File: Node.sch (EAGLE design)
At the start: 69 parts, among them J1 AVR_SPI_PRG_6NS, J2 M04X2, Q1 PMR280UN, Q2 PMR280UN, Q3 PMR280UN, U1 ATMEGA32U4, U2 BLUETOOTH-RN41", U4 L3GD20, U9 RCLAMP0502A, X1 USBSMD

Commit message: more routing
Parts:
- L1, L2: device adjacent-reality:INDUCTORVLS2016 -> adjacent-reality:INDUCTORVLS30
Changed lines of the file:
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@@
 <part name="C23" library="SparkFun" deviceset="CAP" device="0402-CAP" value="1uF"/>
 <part name="U$6" library="adjacent-reality" deviceset="LSM303DLHC" device=""/>
-<part name="L1" library="adjacent-reality" deviceset="INDUCTOR" device="VLS2016" value="4.7uH"/>
-<part name="L2" library="adjacent-reality" deviceset="INDUCTOR" device="VLS2016" value="4.7uH"/>
+<part name="L1" library="adjacent-reality" deviceset="INDUCTOR" device="VLS30" value="4.7uH"/>
+<part name="L2" library="adjacent-reality" deviceset="INDUCTOR" device="VLS30" value="4.7uH"/>
 <part name="JP1" library="SparkFun-Connectors" deviceset="M02" device="PTH" value="POWER"/>
 </parts>

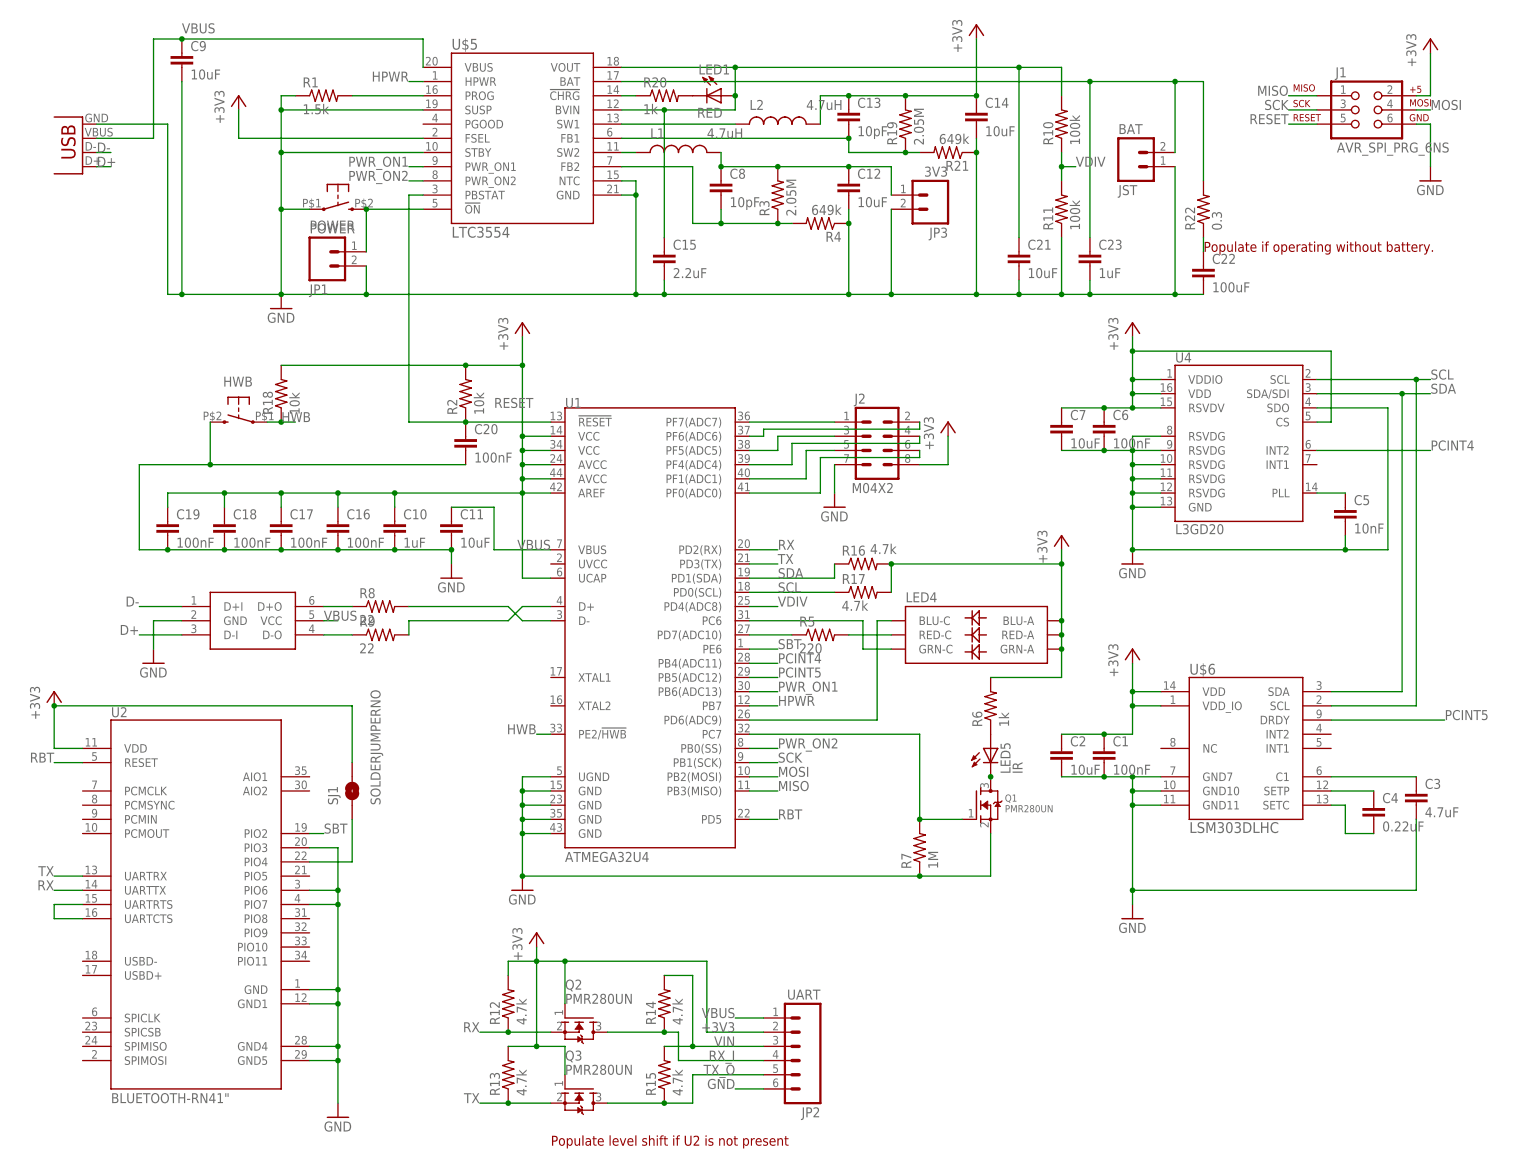
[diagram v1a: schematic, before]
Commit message: labels on top layer
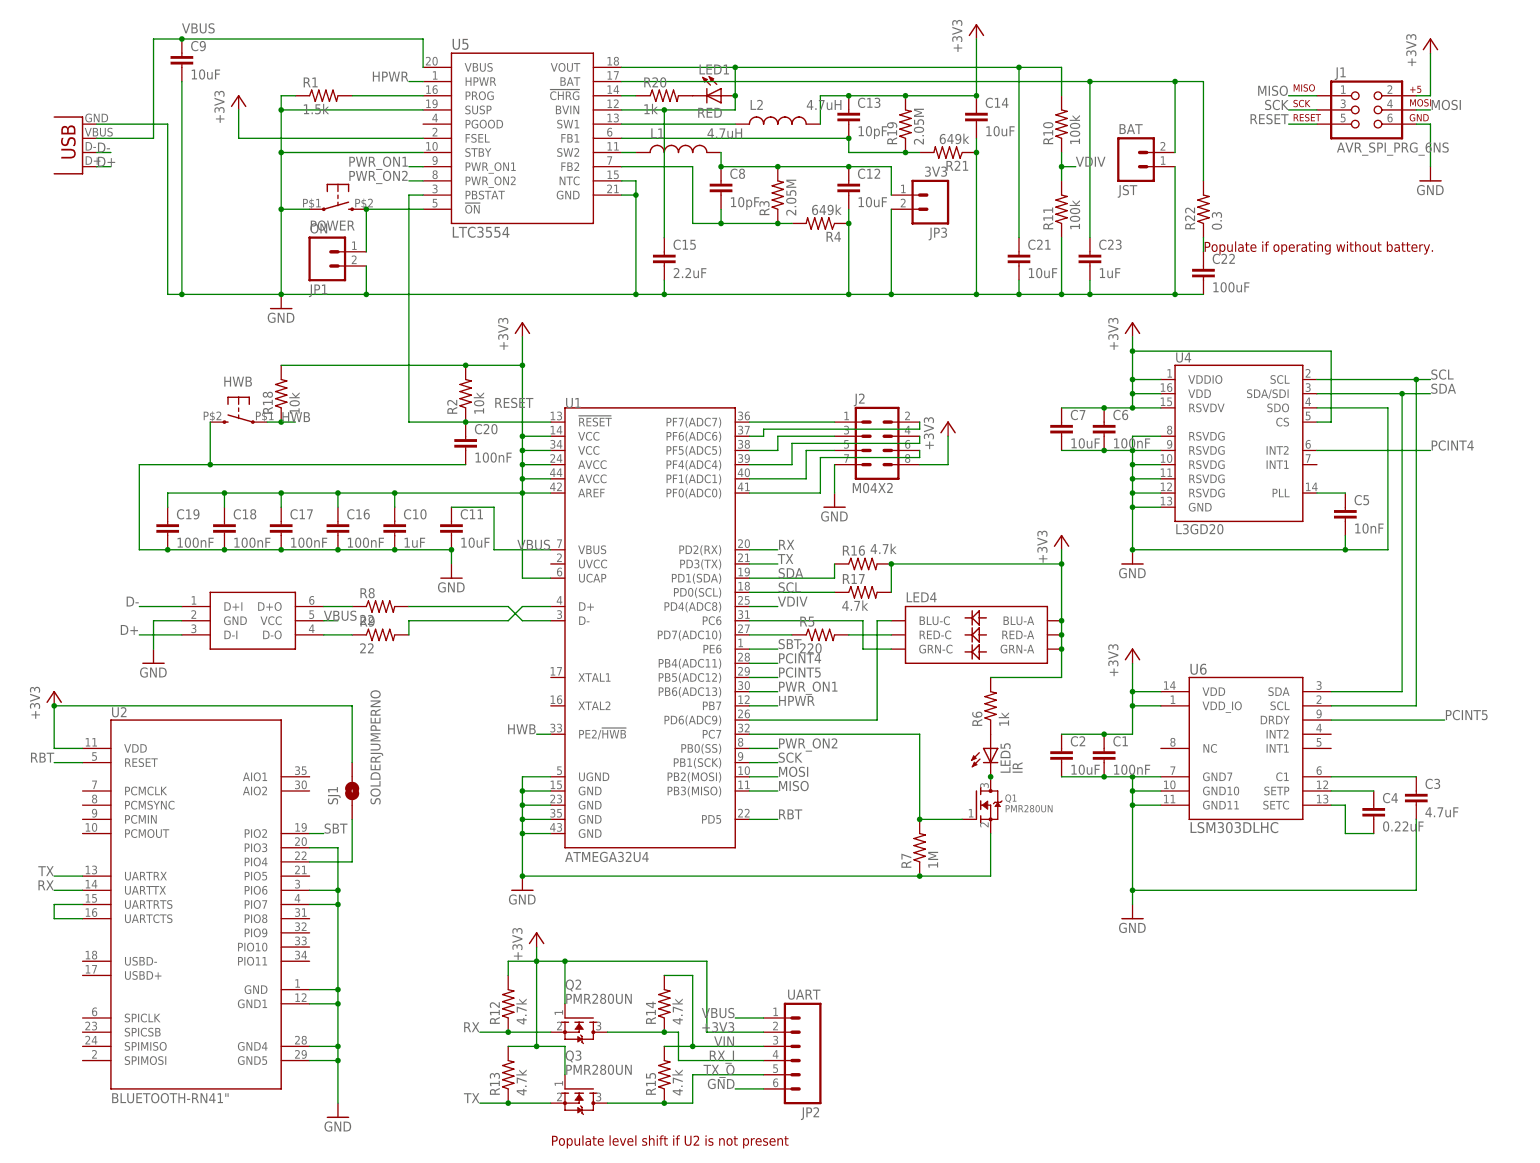
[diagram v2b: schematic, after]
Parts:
- JP1: value POWER -> ON
- renumbered U$5 to U5, U$6 to U6

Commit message: cleanup for rev3 and use ltc3553
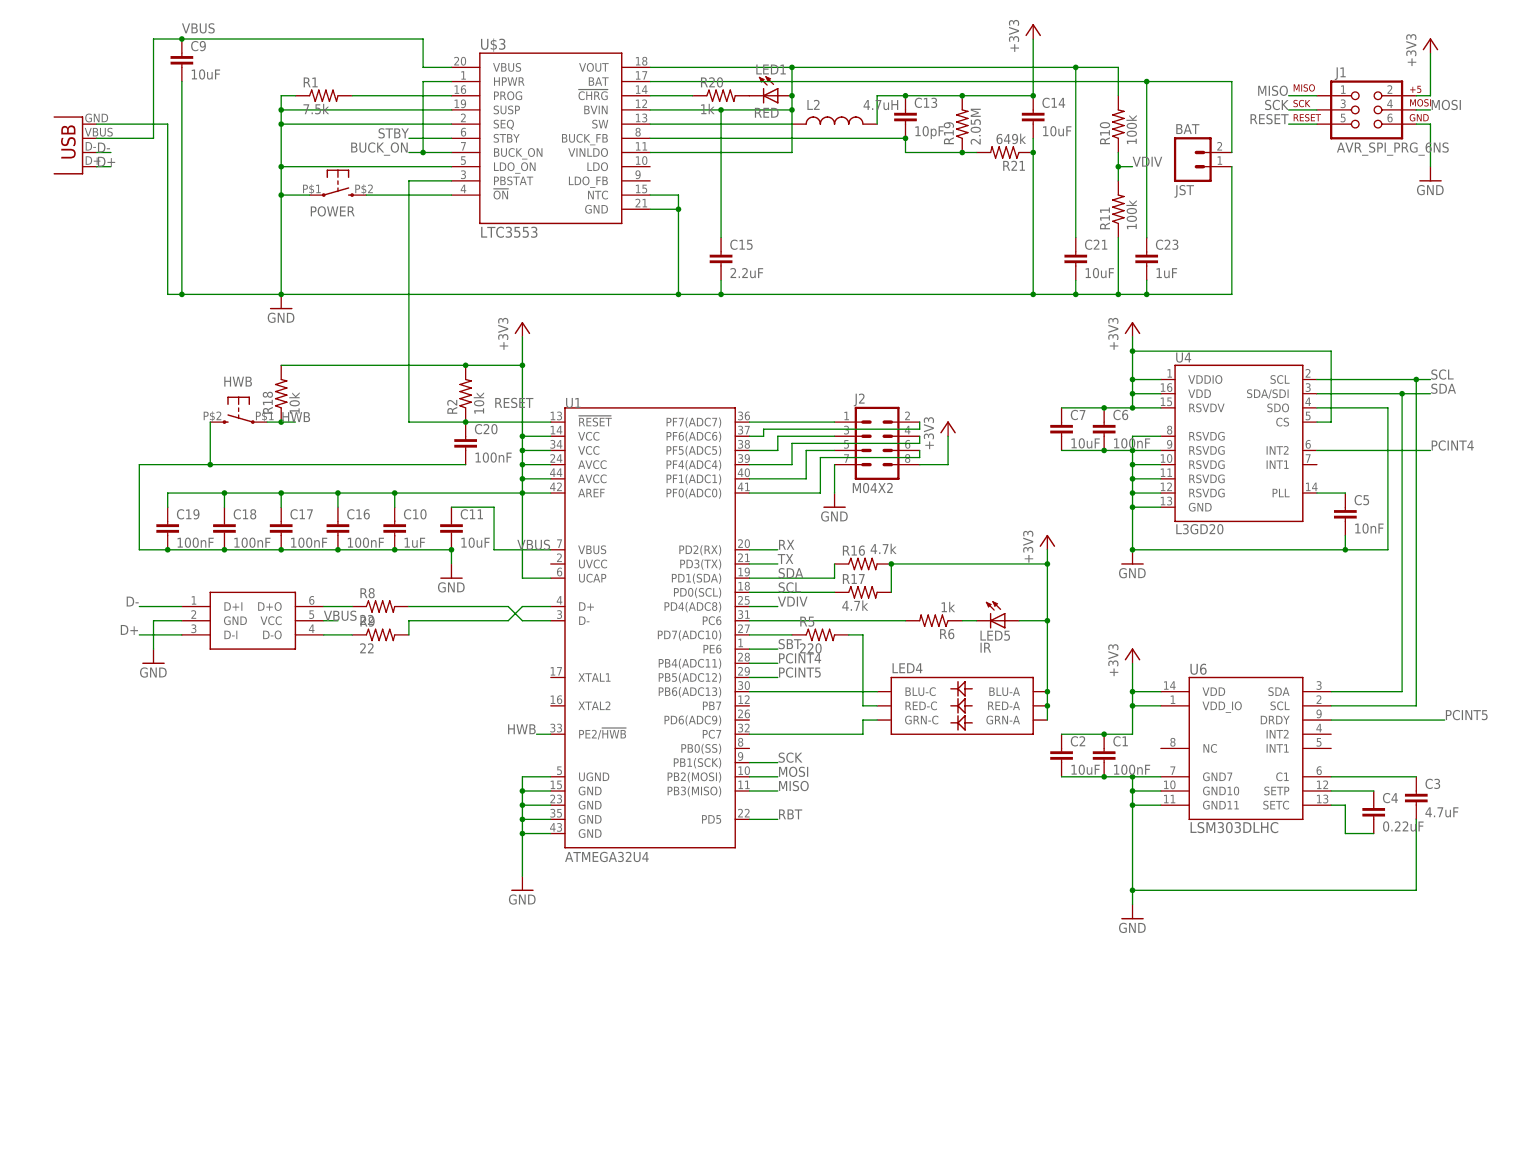
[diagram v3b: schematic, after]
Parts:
- removed C12: 10uF, SparkFun:CAP0603-CAP
- removed C22: 100uF, SparkFun:CAP1210
- removed C8: 10pF, SparkFun:CAP0402-CAP
- removed JP1: ON, SparkFun-Connectors:M02PTH
- removed JP2: UART, SparkFun:M06SIP
- removed JP3: 3V3, SparkFun-Connectors:M02PTH
- removed L1: 4.7uH, adjacent-reality:INDUCTORVLS30
- removed Q1, Q2, Q3: PMR280UN, adjacent-reality:MOSFET-N
- removed R12, R13, R14, R15: 4.7k, SparkFun:RESISTOR0402-RES
- removed R22: 0.3, SparkFun:RESISTOR0603-RES
- removed R3: 2.05M, SparkFun:RESISTOR0402-RES
- removed R4: 649k, SparkFun:RESISTOR0402-RES
- removed R7: 1M, SparkFun:RESISTOR0402-RES
- removed SJ1: SOLDERJUMPERNO, SparkFun:SOLDERJUMPERNO
- removed U2: BLUETOOTH-RN41", adjacent-reality:BLUETOOTH-RN41"
- removed U5: LTC3554, adjacent-reality:LTC3554
- added U$3: LTC3553, adjacent-reality:LTC3553
- R1: value 1.5k -> 7.5k
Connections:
- removed net HPWR: U1.PB7, U5.HPWR
- removed net N$14: SJ1.1, U2.PIO4
- removed net N$19: C12.1, C8.1, JP3.1, L1.2, R3.2
- removed net N$20: LED5.C, Q1.D
- removed net N$22: Q1.G, R7.2, U1.PC7
- removed net N$23: L1.1, U5.SW2
- removed net N$31: C8.2, R3.1, R4.2, U5.FB2
- removed net N$36: C22.1, R22.1
- removed net N$9 (its old number): U2.UARTCTS, U2.UARTRTS
- removed net PWR_ON1: U1.PB6(ADC13), U5.PWR_ON1
- removed net PWR_ON2: U1.PB0(SS), U5.PWR_ON2
- removed net RX_I: JP2.4, Q2.D, R14.1
- removed net TX_O: JP2.5, Q3.D, R15.1
- removed net VIN: JP2.3, R14.2, R15.2
- new net BUCK_ON: U$3.HPWR
- new net N$10: LED5.C, R6.1
- new net STBY: U$3.STBY
- net +3V3: now also LED5.A; no longer JP2.2, Q2.G, Q3.G, R12.2, R13.2, R6.2, SJ1.2, U2.VDD, U5.FSEL
- net GND: now also U$3.GND, U$3.LDO_ON, U$3.NTC, U$3.SEQ, U$3.SUSP; no longer C12.2, C22.2, JP1.2, JP2.6, JP3.2, Q1.S, R4.1, R7.1, U2.GND, U2.GND1, U2.GND4, U2.GND5, U2.PIO3, U2.PIO6, U2.PIO7, U5.GND, U5.NTC, U5.STBY, U5.SUSP
- net N$1: now also U$3.BVIN, U$3.VINLDO, U$3.VOUT; no longer U5.BVIN, U5.VOUT
- net N$12: now also U1.PC7; no longer U1.PC6
- net N$16: now also U$3.!CHRG; no longer U5.!CHRG
- net N$17: now also U1.PB6(ADC13); no longer U1.PD6(ADC9)
- net N$2: now also U$3.PROG; no longer U5.PROG
- net N$27: now also U$3.SW; no longer U5.SW1
- net N$29: now also U$3.BAT; no longer R22.2, U5.BAT
- net N$37: now also U$3.BUCK_FB; no longer U5.FB1
- net N$4: now also R6.2, U1.PC6; no longer LED5.A, R6.1
- net N$8: no longer JP1.1, U5.!ON
- net RBT: no longer U2.RESET
- net RESET: no longer U5.PBSTAT
- net RX: no longer Q2.S, R12.1, U2.UARTTX
- net SBT: no longer U2.PIO2
- net TX: no longer Q3.S, R13.1, U2.UARTRX
- net VBUS: now also U$3.VBUS; no longer JP2.1, U5.VBUS
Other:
- note removed: "Populate if operating without battery."
- note removed: "Populate level shift if U2 is not present"
- moved on the sheet: BAT, C13, C14, C15, C21, C23, L2, LED1, LED4, LED5, POWER, R10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

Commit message: add header and crystal
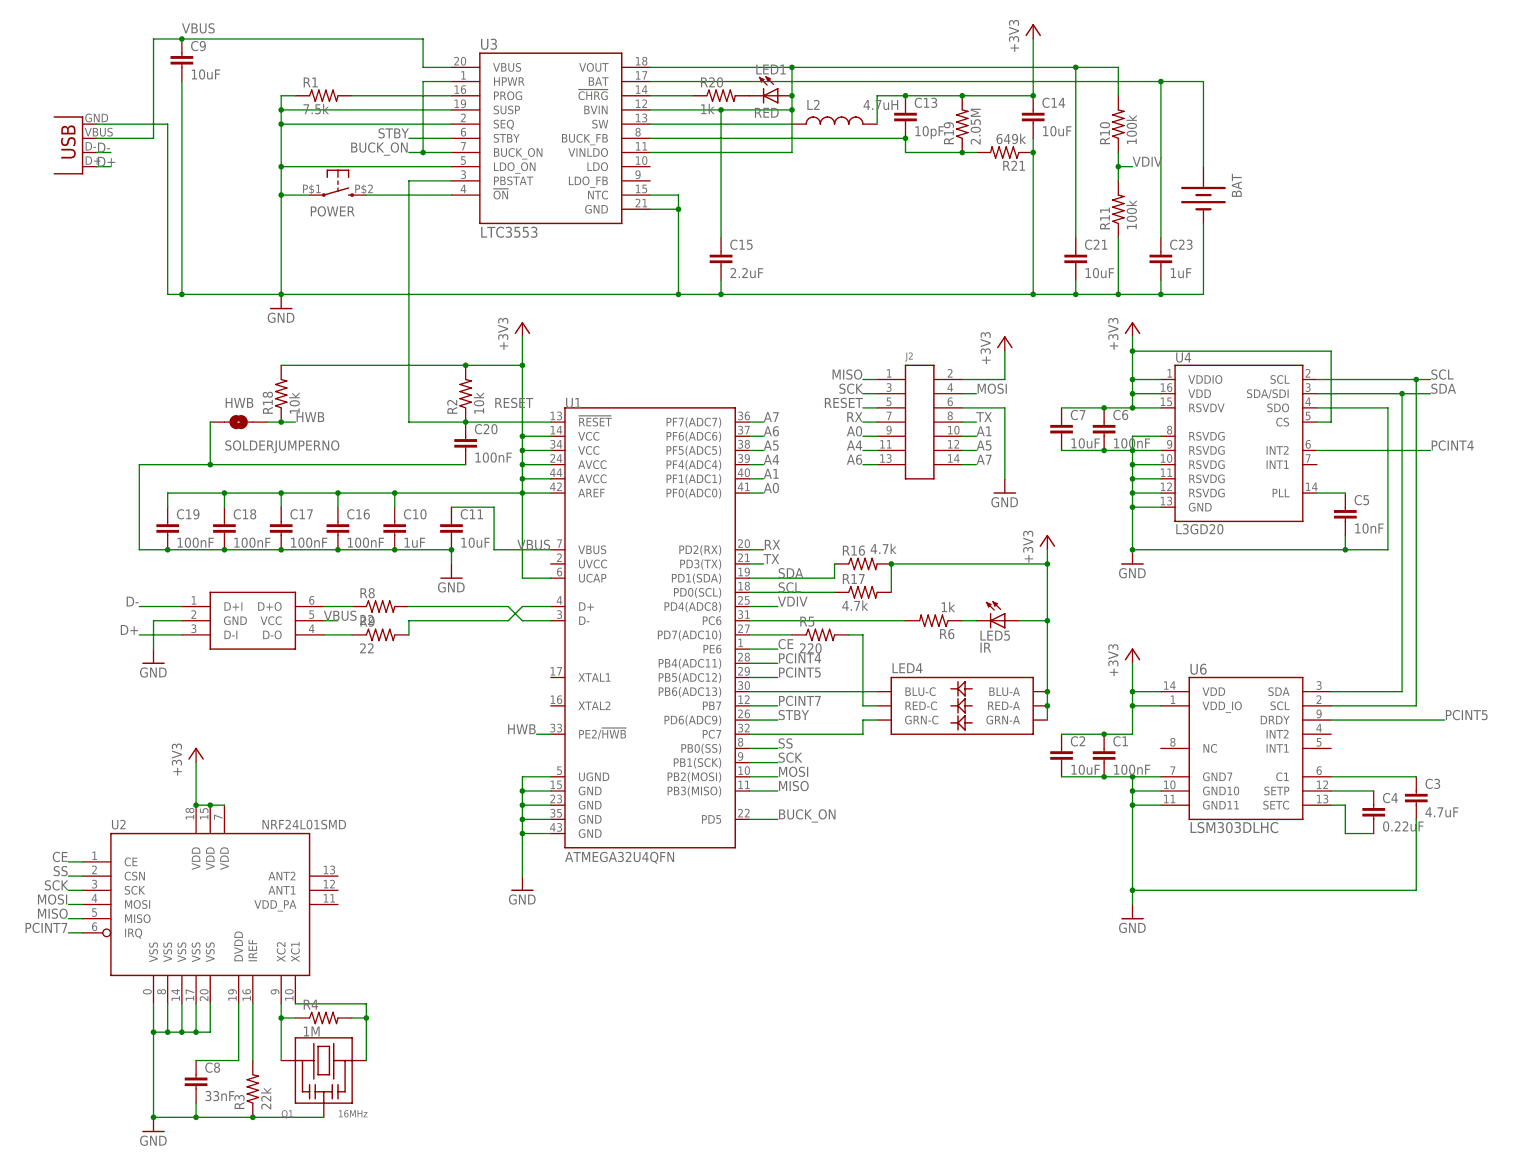
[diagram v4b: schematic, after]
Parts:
- removed J1: AVR_SPI_PRG_6NS, SparkFun:AVR_SPI_PRG_6NS
- added C8: 33nF, SparkFun:CAP0402-CAP
- added Q1: 16MHz, adjacent-reality:RESONATORPRQC
- added R3: 22k, SparkFun:RESISTOR0402-RES
- added R4: 1M, SparkFun:RESISTOR0402-RES
- added U2: NRF24L01SMD, SparkFun-RF:NRF24L01SMD
- BAT: value JST -> (none); device SparkFun:M02-JST-2MM-SMT -> SparkFun-Electromechanical:BATTERY245PTH
- HWB: value KSS -> SOLDERJUMPERNO; device adjacent-reality:KSS -> SparkFun-Passives:SOLDERJUMPERNO
- J2: value M04X2 -> DF12A3.0-14DS; device SparkFun:M04X2 -> adjacent-reality:DF12A3.0-14DS
- U1: value ATMEGA32U4 -> ATMEGA32U4QFN; device adjacent-reality:ATMEGA32U4 -> adjacent-reality:ATMEGA32U4QFN
- renumbered U$3 to U3
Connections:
- removed net N$28: J2.1, U1.PF7(ADC7)
- removed net N$30: J2.2, U1.PF6(ADC6)
- removed net N$32: J2.3, U1.PF5(ADC5)
- removed net N$33: J2.4, U1.PF4(ADC4)
- removed net N$34: J2.5, U1.PF1(ADC1)
- removed net N$35: J2.6, U1.PF0(ADC0)
- removed net RBT: U1.PD5
- removed net SBT: U1.PE6
- new net A0: J2.9, U1.PF0(ADC0)
- new net A1: J2.10, U1.PF1(ADC1)
- new net A4: J2.11, U1.PF4(ADC4)
- new net A5: J2.12, U1.PF5(ADC5)
- new net A6: J2.13, U1.PF6(ADC6)
- new net A7: J2.14, U1.PF7(ADC7)
- new net CE: U1.PE6, U2.CE
- new net N$11: C8.1, U2.DVDD
- new net N$14: R3.2, U2.IREF
- new net N$19: Q1.1, R4.1, U2.XC2
- new net N$20: Q1.2, R4.2, U2.XC1
- new net PCINT7: U1.PB7, U2.IRQ
- new net SS: U1.PB0(SS), U2.CSN
- net +3V3: now also J2.2, U2.VDD@15, U2.VDD@18, U2.VDD@7; no longer J1.2, J2.8
- net BUCK_ON: now also U1.PD5
- net GND: now also BAT.-, C8.2, HWB.1, J2.6, Q1.GND, R3.1, U2.VSS@0, U2.VSS@14, U2.VSS@17, U2.VSS@20, U2.VSS@8; no longer BAT.1, HWB.3, J1.6, J2.7
- net HWB: now also HWB.2; no longer HWB.1
- net MISO: now also J2.1, U2.MISO; no longer J1.1
- net MOSI: now also J2.4, U2.MOSI; no longer J1.4
- net N$29: now also BAT.+; no longer BAT.2
- net RESET: now also J2.5; no longer J1.5
- net RX: now also J2.7
- net SCK: now also J2.3, U2.SCK; no longer J1.3
- net STBY: now also U1.PD6(ADC9)
- net TX: now also J2.8
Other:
- moved on the sheet: C23
